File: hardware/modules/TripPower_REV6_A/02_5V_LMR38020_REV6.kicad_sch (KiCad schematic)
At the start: 16 parts, among them Q501 BVSS123LT1G PGOOD STATUS OPEN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, U101 LMR38020SQDDARQ1

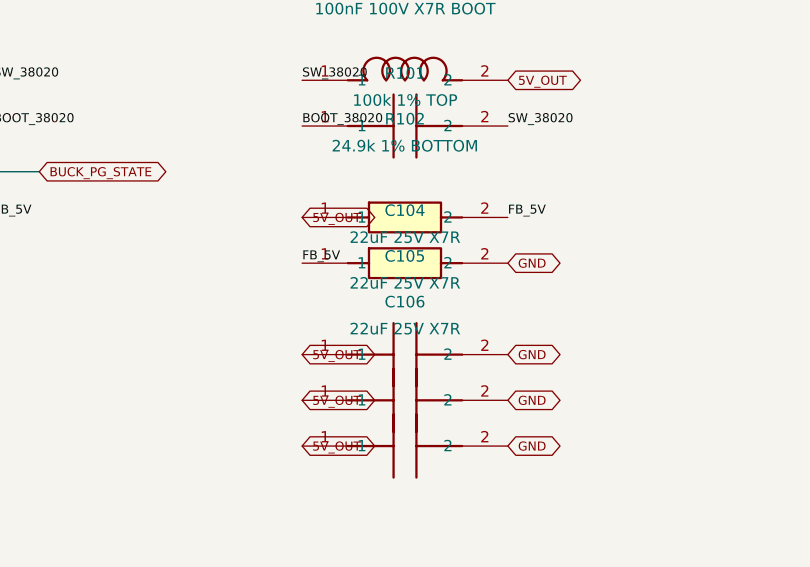
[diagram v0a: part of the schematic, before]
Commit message: REV6 A: replace three EOL Murata 22uF MLCC with stocked automotive AEC-Q200 Taiyo Yuden MCAST32MSB7226KPNA01
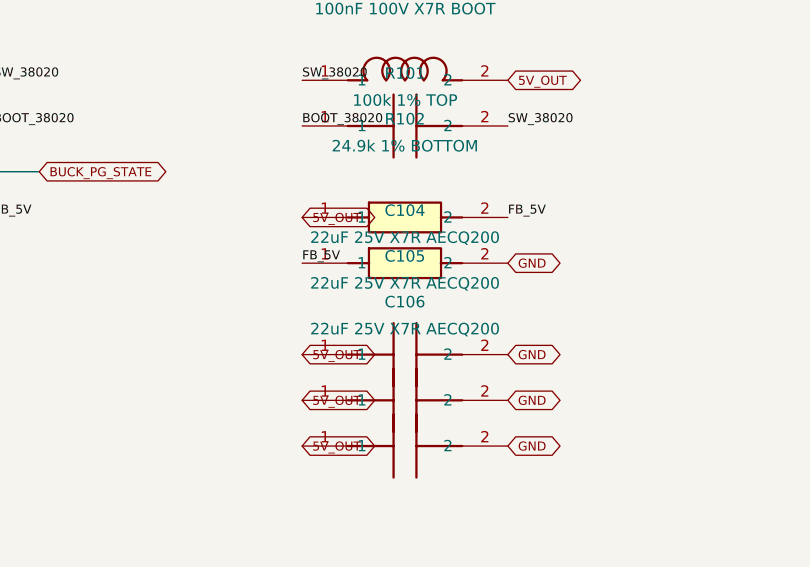
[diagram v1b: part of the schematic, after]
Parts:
- C104, C105, C106: value 22uF 25V X7R -> 22uF 25V X7R AECQ200; MPN GRM32ER71E226KE15L -> MCAST32MSB7226KPNA01

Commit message: REV6 A: add non-BOM 5V_OUT sense testpoint TP502 on native buck sheet without incorrectly claiming 2A connector rating
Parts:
- added TP502: MAIN_5V_SENSE_ONLY_NOT_2A_CONNECTOR, TestPoint:TestPoint_Pad_1.5x1.5mm, symbol TripPower_PGOOD:SignalPad
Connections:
- net 5V_OUT: now also TP502.1 (PAD)
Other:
- note added: "TP502 is a diagnostic sense-only pad. MAIN 5V/2A must use a separately qualified board-to-board 2A carrier connector/land pattern; no 2A testpad claim."

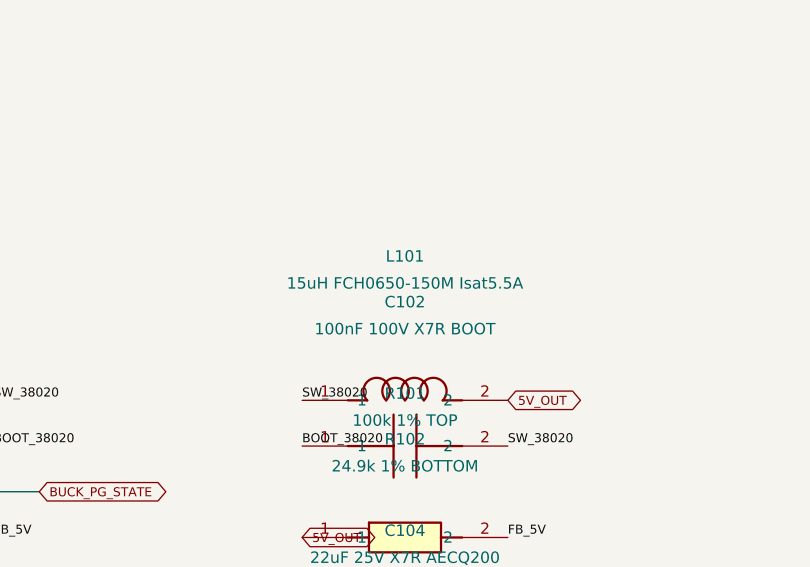
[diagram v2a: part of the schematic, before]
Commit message: REV6 A: replace weakly documented Fangcheng L101 with Bourns SRP7050TA-150M AEC-Q200 Isat6A documented footprint
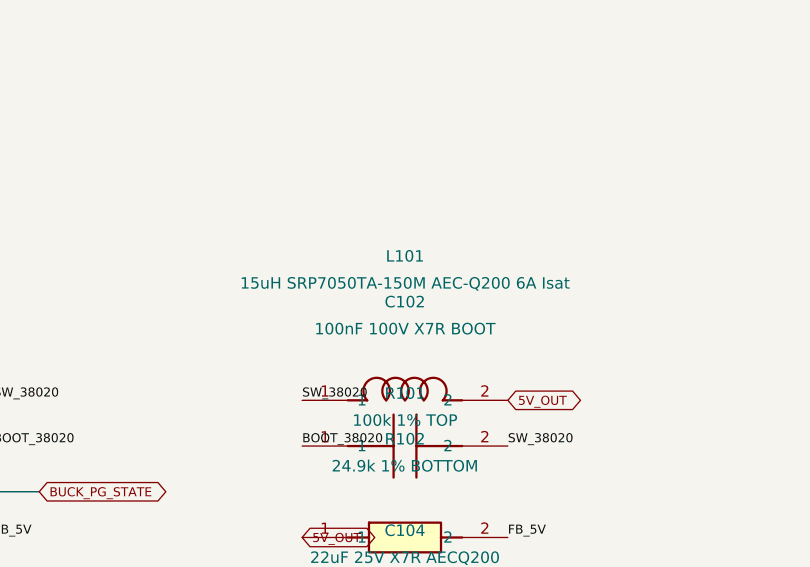
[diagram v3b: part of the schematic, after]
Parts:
- L101: value 15uH FCH0650-150M Isat5.5A -> 15uH SRP7050TA-150M AEC-Q200 6A Isat; footprint Tripmaster:L_FANGCHENG_FCH0650_150M -> Tripmaster:L_Bourns_SRP7050TA_150M; MPN FCH0650-150M -> SRP7050TA-150M
